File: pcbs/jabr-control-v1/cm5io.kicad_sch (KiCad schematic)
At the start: 5 parts, among them J10001 ARJM11D7-502-AB-EW2, J10002 TYPE-C-31-M-12, U2401 PESD4USB3BTTS-QX, U2402 PESD4USB3BTTS-QX

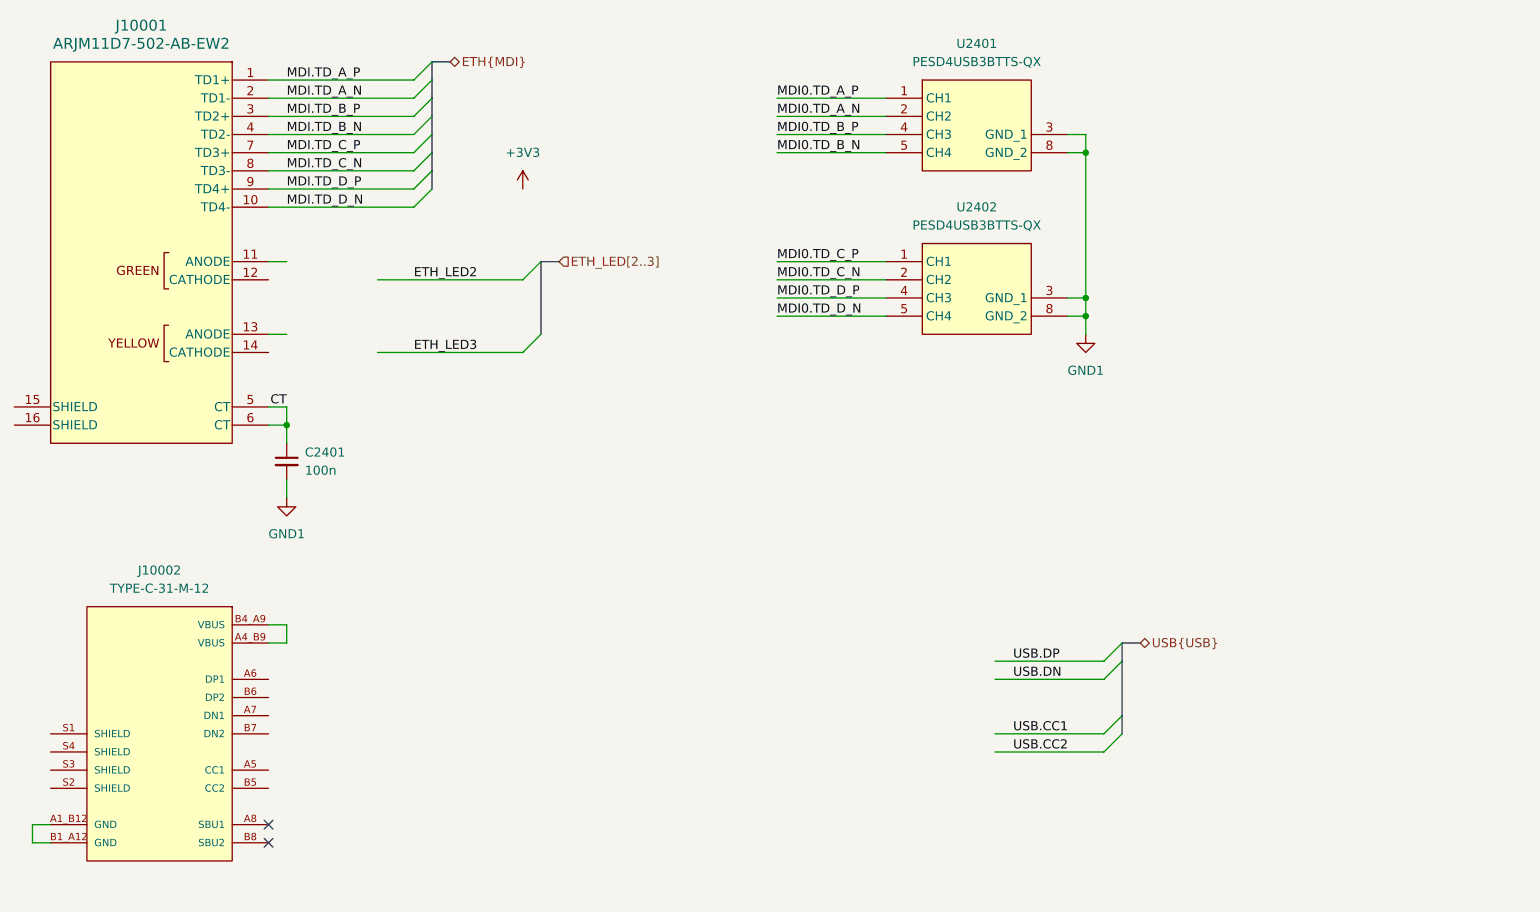
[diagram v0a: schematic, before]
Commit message: Added power sheets
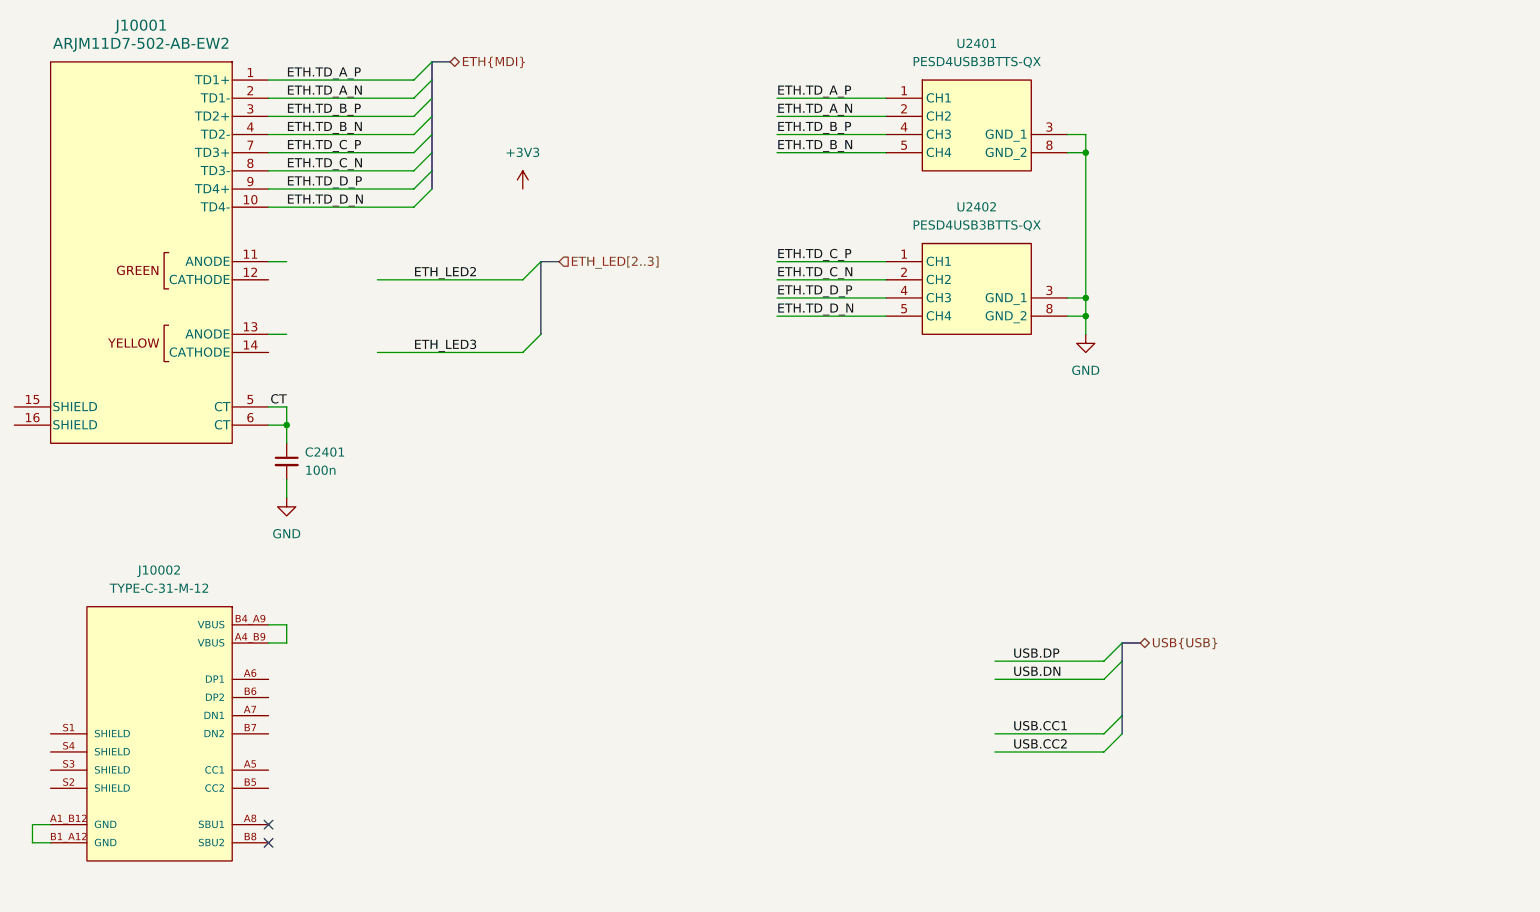
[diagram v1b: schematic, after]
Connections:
- net MDI0.TD_A_N is gone; now on net ETH.TD_A_N: U2401.2 (CH2), U2401.9 (NC)
- net MDI0.TD_A_P is gone; now on net ETH.TD_A_P: U2401.1 (CH1), U2401.10 (NC)
- net MDI0.TD_B_N is gone; now on net ETH.TD_B_N: U2401.5 (CH4), U2401.6 (NC)
- net MDI0.TD_B_P is gone; now on net ETH.TD_B_P: U2401.4 (CH3), U2401.7 (NC)
- net MDI0.TD_C_N is gone; now on net ETH.TD_C_N: U2402.2 (CH2), U2402.9 (NC)
- net MDI0.TD_C_P is gone; now on net ETH.TD_C_P: U2402.1 (CH1), U2402.10 (NC)
- net MDI0.TD_D_N is gone; now on net ETH.TD_D_N: U2402.5 (CH4), U2402.6 (NC)
- net MDI0.TD_D_P is gone; now on net ETH.TD_D_P: U2402.4 (CH3), U2402.7 (NC)
- net GND1 renamed GND
- net MDI.TD_A_N renamed ETH.TD_A_N
- net MDI.TD_A_P renamed ETH.TD_A_P
- net MDI.TD_B_N renamed ETH.TD_B_N
- net MDI.TD_B_P renamed ETH.TD_B_P
- net MDI.TD_C_N renamed ETH.TD_C_N
- net MDI.TD_C_P renamed ETH.TD_C_P
- net MDI.TD_D_N renamed ETH.TD_D_N
- net MDI.TD_D_P renamed ETH.TD_D_P
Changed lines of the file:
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@@
 		)
 	)
-	(label "MDI0.TD_B_N"
+	(label "ETH.TD_B_P"
+		(at 165.1 43.18 0)
+		(effects
+			(font
+				(size 1.27 1.27)
+			)
+			(justify left bottom)
+		)
+	)
+	(label "ETH.TD_A_N"
+		(at 165.1 40.64 0)
+		(effects
+			(font
+				(size 1.27 1.27)
+			)
+			(justify left bottom)
+		)
+	)
+	(label "ETH.TD_D_N"
+		(at 96.52 53.34 0)
+		(effects
+			(font
+				(size 1.27 1.27)
+			)
+			(justify left bottom)
+		)
+	)
+	(label "ETH.TD_B_N"
 		(at 165.1 45.72 0)
 		(effects
@@
 		)
 	)
-	(label "MDI.TD_D_N"
-		(at 96.52 53.34 0)
-		(effects
-			(font
-				(size 1.27 1.27)
-			)
-			(justify left bottom)
-		)
-	)
-	(label "MDI.TD_A_P"
+	(label "ETH.TD_A_P"
 		(at 96.52 35.56 0)
 		(effects
@@
 		)
 	)
+	(label "ETH.TD_D_N"
+		(at 165.1 68.58 0)
+		(effects
+			(font
+				(size 1.27 1.27)
+			)
+			(justify left bottom)
+		)
+	)
+	(label "ETH.TD_A_P"
+		(at 165.1 38.1 0)
+		(effects
+			(font
+				(size 1.27 1.27)
+			)
+			(justify left bottom)
+		)
+	)
 	(label "USB.DP"
 		(at 198.12 116.84 0)
@@
 		)
 	)
-	(label "MDI0.TD_D_N"
-		(at 165.1 68.58 0)
-		(effects
-			(font
-				(size 1.27 1.27)
-			)
-			(justify left bottom)
-		)
-	)
-	(label "MDI0.TD_C_N"
-		(at 165.1 63.5 0)
-		(effects
-			(font
-				(size 1.27 1.27)
-			)
-			(justify left bottom)
-		)
-	)
-	(label "MDI0.TD_B_P"
-		(at 165.1 43.18 0)
-		(effects
-			(font
-				(size 1.27 1.27)
-			)
-			(justify left bottom)
-		)
-	)
-	(label "MDI.TD_B_N"
+	(label "ETH.TD_B_N"
 		(at 96.52 43.18 0)
 		(effects
@@
 		)
 	)
-	(label "MDI.TD_C_N"
+	(label "ETH.TD_C_N"
 		(at 96.52 48.26 0)
 		(effects
@@
 		)
 	)
-	(label "MDI.TD_C_P"
+	(label "ETH.TD_C_P"
 		(at 96.52 45.72 0)
-		(effects
-			(font
-				(size 1.27 1.27)
-			)
-			(justify left bottom)
-		)
-	)
-	(label "MDI0.TD_A_P"
-		(at 165.1 38.1 0)
 		(effects
 			(font
@@
 		)
 	)
+	(label "ETH.TD_C_P"
+		(at 165.1 60.96 0)
+		(effects
+			(font
+				(size 1.27 1.27)
+			)
+			(justify left bottom)
+		)
+	)
 	(label "USB.CC1"
 		(at 198.12 127 0)
@@
 		)
 	)
-	(label "MDI0.TD_C_P"
-		(at 165.1 60.96 0)
-		(effects
-			(font
-				(size 1.27 1.27)
-			)
-			(justify left bottom)
-		)
-	)
 	(label "ETH_LED2"
 		(at 114.3 63.5 0)
@@
 		)
 	)
-	(label "MDI.TD_D_P"
+	(label "ETH.TD_D_P"
 		(at 96.52 50.8 0)
 		(effects
@@
 		)
 	)
-	(label "MDI0.TD_A_N"
-		(at 165.1 40.64 0)
-		(effects
-			(font
-				(size 1.27 1.27)
-			)
-			(justify left bottom)
-		)
-	)
-	(label "MDI.TD_A_N"
+	(label "ETH.TD_C_N"
+		(at 165.1 63.5 0)
+		(effects
+			(font
+				(size 1.27 1.27)
+			)
+			(justify left bottom)
+		)
+	)
+	(label "ETH.TD_A_N"
 		(at 96.52 38.1 0)
 		(effects
@@
 		)
 	)
-	(label "MDI.TD_B_P"
+	(label "ETH.TD_D_P"
+		(at 165.1 66.04 0)
+		(effects
+			(font
+				(size 1.27 1.27)
+			)
+			(justify left bottom)
+		)
+	)
+	(label "ETH.TD_B_P"
 		(at 96.52 40.64 0)
 		(effects
@@
 	(label "USB.DN"
 		(at 198.12 119.38 0)
-		(effects
-			(font
-				(size 1.27 1.27)
-			)
-			(justify left bottom)
-		)
-	)
-	(label "MDI0.TD_D_P"
-		(at 165.1 66.04 0)
 		(effects
 			(font
@@
 	)
 	(symbol
-		(lib_id "power:GND1")
+		(lib_id "power:GND")
 		(at 208.28 71.12 0)
 		(mirror y)
@@
 		(dnp no)
 		(fields_autoplaced yes)
-		(property "Reference" "#PWR02415"
+		(property "Reference" "#PWR2415"
 			(at 208.28 77.47 0)
 			(effects
@@
 			)
 		)
-		(property "Value" "GND1"
+		(property "Value" "GND"
 			(at 208.28 76.2 0)
 			(effects
@@
 			)
 		)
-		(property "Description" "Power symbol creates a global label with name \"GND1\" , ground"
+		(property "Description" "Power symbol creates a global label with name \"GND\" , ground"
 			(at 208.28 71.12 0)
 			(effects
@@
 			(project "jabr-control-v1"
 				(path "/f91ec272-d09a-4038-bbbb-962739a92c51/adc0b005-3094-4656-96e7-4ee9fb2ab719"
-					(reference "#PWR02415")
+					(reference "#PWR2415")
 					(unit 1)
 				)
@@
 	)
 	(symbol
-		(lib_id "power:GND1")
+		(lib_id "power:GND")
 		(at 96.52 93.98 0)
 		(unit 1)
@@
 		(dnp no)
 		(fields_autoplaced yes)
-		(property "Reference" "#PWR02405"
+		(property "Reference" "#PWR2405"
 			(at 96.52 100.33 0)
 			(effects
@@
 			)
 		)
-		(property "Value" "GND1"
+		(property "Value" "GND"
 			(at 96.52 99.06 0)
 			(effects
@@
 			)
 		)
-		(property "Description" "Power symbol creates a global label with name \"GND1\" , ground"
+		(property "Description" "Power symbol creates a global label with name \"GND\" , ground"
 			(at 96.52 93.98 0)
 			(effects
@@
 			(project "jabr-control-v1"
 				(path "/f91ec272-d09a-4038-bbbb-962739a92c51/adc0b005-3094-4656-96e7-4ee9fb2ab719"
-					(reference "#PWR02405")
+					(reference "#PWR2405")
 					(unit 1)
 				)

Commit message: Worked on power and other areas of the schematic
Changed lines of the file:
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@@
 	(generator_version "9.0")
 	(paper "A4")
+	(text_box "Dual USB3 type A"
+		(exclude_from_sim no)
+		(at 132.08 121.92 0)
+		(size 30.48 27.94)
+		(margins 0.9525 0.9525 0.9525 0.9525)
+		(stroke
+			(width 0)
+			(type solid)
+			(color 255 0 0 1)
+		)
+		(fill
+			(type none)
+		)
+		(effects
+			(font
+				(size 1.27 1.27)
+				(color 255 0 0 1)
+			)
+			(justify left top)
+		)
+	)
 	(junction
 		(at 208.28 45.72)

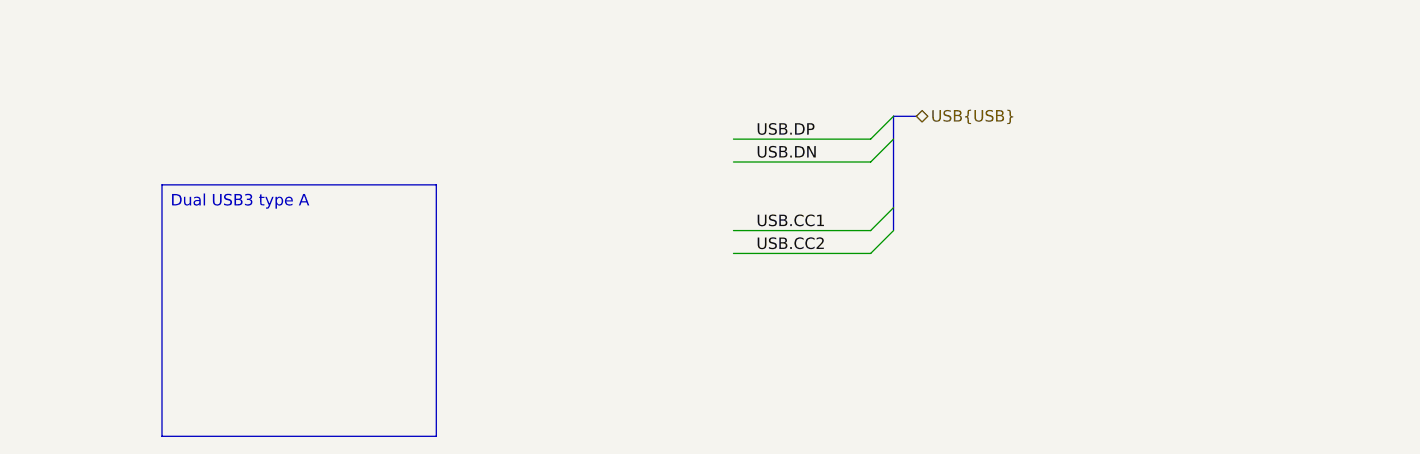
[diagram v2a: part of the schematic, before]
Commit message: Finished M.2 E-Key schematic
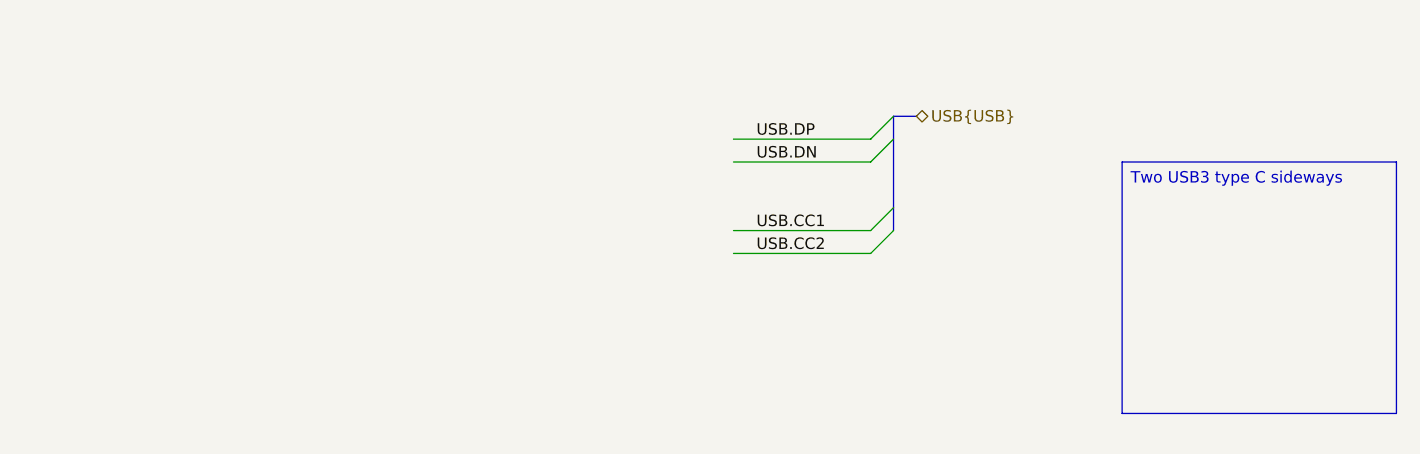
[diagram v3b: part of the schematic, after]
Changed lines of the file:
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@@
 	(generator_version "9.0")
 	(paper "A4")
-	(text_box "Dual USB3 type A"
+	(text_box "Two USB3 type C sideways"
 		(exclude_from_sim no)
-		(at 132.08 121.92 0)
+		(at 238.76 119.38 0)
 		(size 30.48 27.94)
 		(margins 0.9525 0.9525 0.9525 0.9525)
